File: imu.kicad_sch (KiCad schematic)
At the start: 1 part, among them U6 MPU-6050

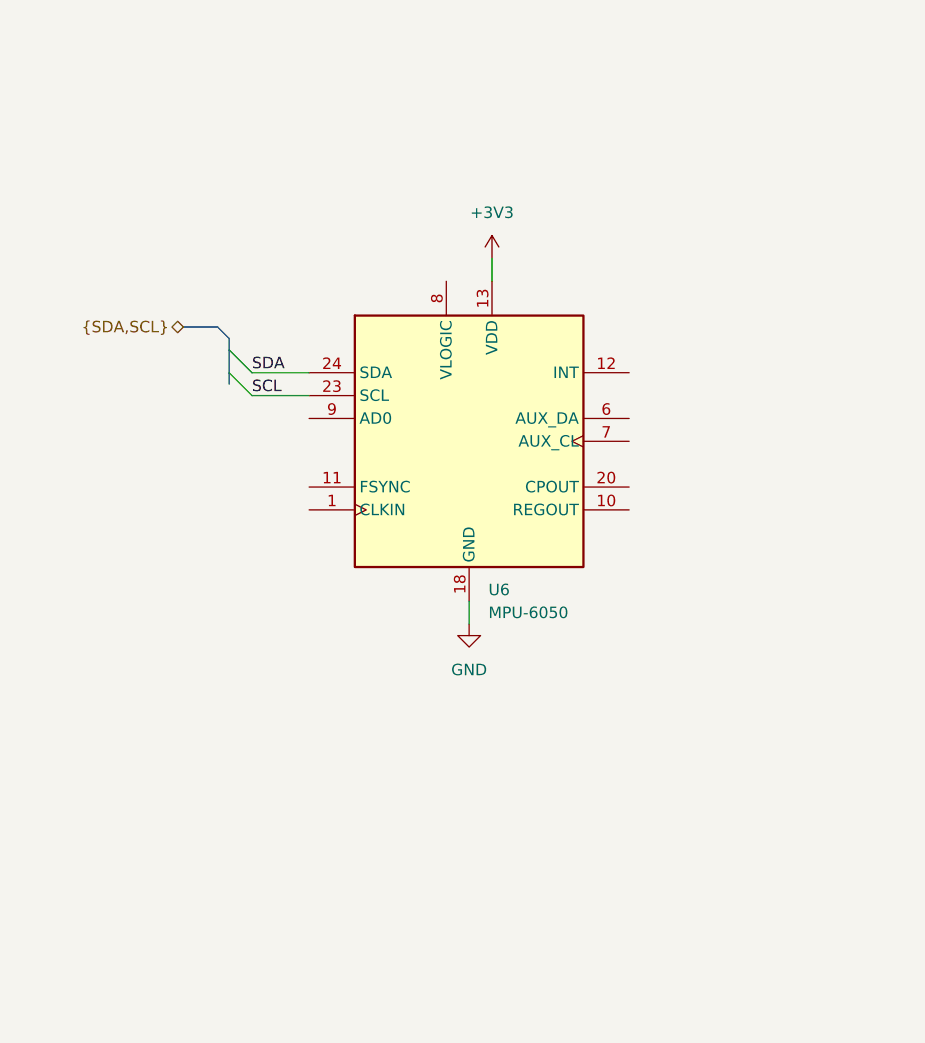
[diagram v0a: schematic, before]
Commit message: update schematic
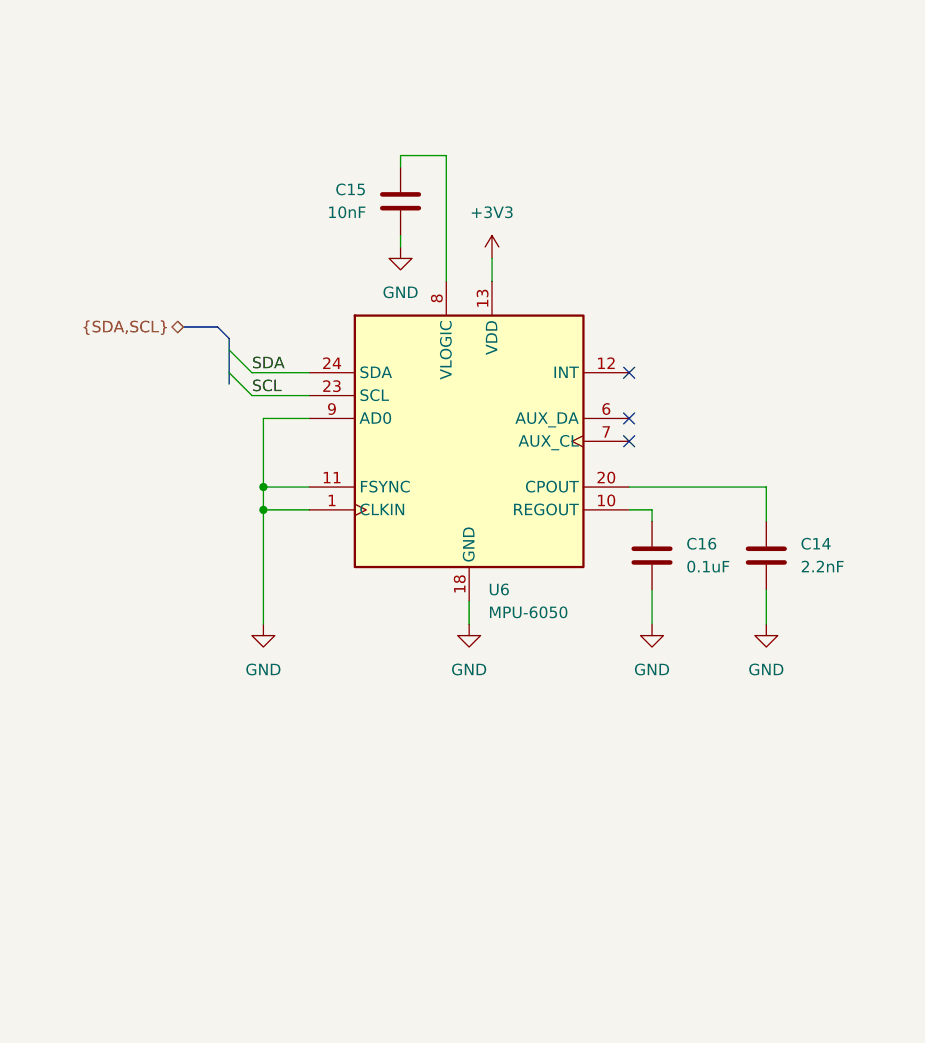
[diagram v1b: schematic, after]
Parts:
- added C14: 2.2nF, symbol Device:C
- added C15: 10nF, symbol Device:C
- added C16: 0.1uF, symbol Device:C
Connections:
- net GND: now also U6.1 (CLKIN), U6.11 (FSYNC), U6.9 (AD0), C14.2, C15.2, C16.2
- net at U6.10 (REGOUT): now also C16.1
- net at U6.20 (CPOUT): now also C14.1
- net at U6.8 (VLOGIC): now also C15.1
- no-connect marks 0 -> 3

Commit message: improve design
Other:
- title: (none) -> Dropbot
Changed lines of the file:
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@@
 	(generator_version "10.0")
 	(paper "A4")
+	(title_block
+		(title "Dropbot")
+	)
 	(junction
 		(at 123.19 93.98)

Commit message: progress on routing
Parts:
- removed C16: 0.1uF, symbol Device:C
- removed U6: MPU-6050, Sensor_Motion:InvenSense_QFN-24_4x4mm_P0.5mm, symbol Sensor_Motion:MPU-6050
- added C29, C30: 100nF, Capacitor_SMD:C_0603_1608Metric, symbol Device:C
- added U1: MMC5983MA, MMC5983MA:PQFN50P300X300X100-16N, symbol MMC5983MA:MMC5983MA
- added U11: BMI270, Package_LGA:Bosch_LGA-14_3x2.5mm_P0.5mm, symbol BMI270:BMI270
- C14: value 2.2nF -> 10uF
- C15: value 10nF -> 10uF
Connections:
- net +3V3: now also C15.1, C29.1, C30.1, U1.13 (VDDIO), U1.2 (VDD), U1.4 (~{SPI_CS}), U11.12 (CSB), U11.5 (VDDIO), U11.8 (VDD)
- net GND: now also C29.2, C30.2, U1.11 (GND), U1.9 (GND), U11.1 (SDO), U11.6 (GNDIO), U11.7 (GND)
- net SCL: now also U1.1 (SCL/SPI_SCK), U11.13 (SCX)
- net SDA: now also U1.16 (SDA/SPI_SDI), U11.14 (SDX)
- net at C14.1: now also U1.10 (CAP)
- new net: U1.12 (NC), U1.14 (NC), U1.3 (NC), U1.6 (NC), U1.7 (NC), U1.8 (NC)
- no-connect marks 3 -> 7

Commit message: progress on routing
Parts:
- C14, C15: footprint (none) -> Capacitor_SMD:C_0603_1608Metric
- U1: footprint MMC5983MA:PQFN50P300X300X100-16N -> Package_LGA:LGA-16_3x3mm_P0.5mm
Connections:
- no-connect marks 7 -> 8
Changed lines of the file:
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@@
+	)
+	(no_connect
+		(at 132.08 71.12)
 	)
 	(no_connect
@@
 			)
 		)
-		(property "Footprint" ""
+		(property "Footprint" "Capacitor_SMD:C_0603_1608Metric"
 			(at 171.1452 71.12 0)
 			(hide yes)
@@
 			)
 		)
-		(property "Footprint" "MMC5983MA:PQFN50P300X300X100-16N"
+		(property "Footprint" "Package_LGA:LGA-16_3x3mm_P0.5mm"
 			(at 146.05 68.58 0)
 			(hide yes)
@@
 			)
 		)
-		(property "Footprint" ""
+		(property "Footprint" "Capacitor_SMD:C_0603_1608Metric"
 			(at 125.4252 85.09 0)
 			(hide yes)

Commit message: tentative automatic population
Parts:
- C14, C15: LCSC (none) -> C962136; MPN (none) -> CL10A106KO8NQNC; Manufacturer (none) -> Samsung Electro-Mechanics
- C29, C30: LCSC (none) -> C14663; MPN (none) -> CC0603KRX7R9BB104; Manufacturer (none) -> YAGEO
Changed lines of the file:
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@@
 			)
 		)
-		(property "Datasheet" ""
+		(property "Datasheet" "https://datasheet.lcsc.com/datasheet/pdf/02336ea48ea44ca18c72517dd3cb7b47.pdf?productCode=C962136"
 			(at 170.18 67.31 0)
 			(hide yes)
@@
 					(size 1.27 1.27)
 				)
+			)
+		)
+		(property "Manufacturer" "Samsung Electro-Mechanics" (at 0 0 0)
+			(effects
+				(font
+					(size 1.27 1.27)
+				)
+				(hide yes)
+			)
+		)
+		(property "MPN" "CL10A106KO8NQNC" (at 0 0 0)
+			(effects
+				(font
+					(size 1.27 1.27)
+				)
+				(hide yes)
+			)
+		)
+		(property "LCSC" "C962136" (at 0 0 0)
+			(effects
+				(font
+					(size 1.27 1.27)
+				)
+				(hide yes)
 			)
 		)
@@
 			)
 		)
-		(property "Datasheet" ""
+		(property "Datasheet" "https://datasheet.lcsc.com/datasheet/pdf/02336ea48ea44ca18c72517dd3cb7b47.pdf?productCode=C962136"
 			(at 124.46 81.28 0)
 			(hide yes)
@@
 					(size 1.27 1.27)
 				)
+			)
+		)
+		(property "Manufacturer" "Samsung Electro-Mechanics" (at 0 0 0)
+			(effects
+				(font
+					(size 1.27 1.27)
+				)
+				(hide yes)
+			)
+		)
+		(property "MPN" "CL10A106KO8NQNC" (at 0 0 0)
+			(effects
+				(font
+					(size 1.27 1.27)
+				)
+				(hide yes)
+			)
+		)
+		(property "LCSC" "C962136" (at 0 0 0)
+			(effects
+				(font
+					(size 1.27 1.27)
+				)
+				(hide yes)
 			)
 		)
@@
 			)
 		)
-		(property "Datasheet" ""
+		(property "Datasheet" "https://datasheet.lcsc.com/datasheet/pdf/23ccee80ee542e7cf156a772bb589942.pdf?productCode=C14663"
 			(at 184.15 115.57 0)
 			(hide yes)
@@
 					(size 1.27 1.27)
 				)
+			)
+		)
+		(property "Manufacturer" "YAGEO" (at 0 0 0)
+			(effects
+				(font
+					(size 1.27 1.27)
+				)
+				(hide yes)
+			)
+		)
+		(property "MPN" "CC0603KRX7R9BB104" (at 0 0 0)
+			(effects
+				(font
+					(size 1.27 1.27)
+				)
+				(hide yes)
+			)
+		)
+		(property "LCSC" "C14663" (at 0 0 0)
+			(effects
+				(font
+					(size 1.27 1.27)
+				)
+				(hide yes)
 			)
 		)
@@
 			)
 		)
-		(property "Datasheet" ""
+		(property "Datasheet" "https://datasheet.lcsc.com/datasheet/pdf/23ccee80ee542e7cf156a772bb589942.pdf?productCode=C14663"
 			(at 171.45 115.57 0)
 			(hide yes)
@@
 			)
 		)
+		(property "Manufacturer" "YAGEO" (at 0 0 0)
+			(effects
+				(font
+					(size 1.27 1.27)
+				)
+				(hide yes)
+			)
+		)
+		(property "MPN" "CC0603KRX7R9BB104" (at 0 0 0)
+			(effects
+				(font
+					(size 1.27 1.27)
+				)
+				(hide yes)
+			)
+		)
+		(property "LCSC" "C14663" (at 0 0 0)
+			(effects
+				(font
+					(size 1.27 1.27)
+				)
+				(hide yes)
+			)
+		)

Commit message: annotate with LCSC components
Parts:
- U1: LCSC (none) -> C404329; MPN (none) -> MMC5983MA; Manufacturer (none) -> MEMSIC
- U11: LCSC (none) -> C2836813; MPN (none) -> BMI270; Manufacturer (none) -> Bosch Sensortec
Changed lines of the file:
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@@
+			)
+		)
+		(property "LCSC" "C404329" (at 0 0 0)
+			(effects
+				(font
+					(size 1.27 1.27)
+				)
+				(hide yes)
+			)
+		)
+		(property "MPN" "MMC5983MA" (at 0 0 0)
+			(effects
+				(font
+					(size 1.27 1.27)
+				)
+				(hide yes)
+			)
+		)
+		(property "Manufacturer" "MEMSIC" (at 0 0 0)
+			(effects
+				(font
+					(size 1.27 1.27)
+				)
+				(hide yes)
 			)
 		)
@@
 			)
 		)
+		(property "LCSC" "C2836813" (at 0 0 0)
+			(effects
+				(font
+					(size 1.27 1.27)
+				)
+				(hide yes)
+			)
+		)
+		(property "MPN" "BMI270" (at 0 0 0)
+			(effects
+				(font
+					(size 1.27 1.27)
+				)
+				(hide yes)
+			)
+		)
+		(property "Manufacturer" "Bosch Sensortec" (at 0 0 0)
+			(effects
+				(font
+					(size 1.27 1.27)
+				)
+				(hide yes)
+			)
+		)
